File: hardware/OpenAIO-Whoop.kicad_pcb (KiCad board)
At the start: 6 copper layers, 30.5 x 30.5 mm, 0 parts

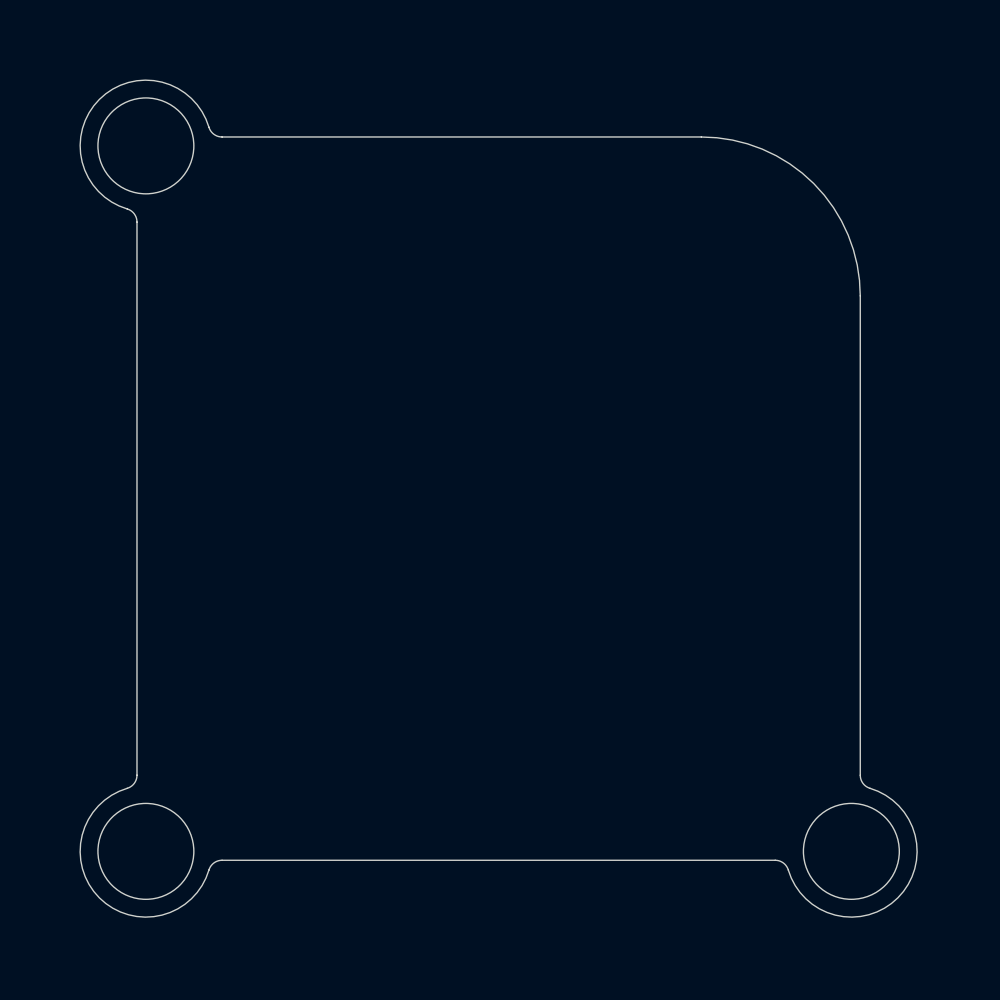
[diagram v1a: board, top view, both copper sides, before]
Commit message: hardware: P2 floorplan run 2 (326/329 placed, 0 spacing, 0 DRC)
Every BOM part placed on its planned side and region with real library
footprints at the 0.2 mm body rule; pad labels, incutec logo and product
name on silk. Compaction with via-in-pad follows.

Co-Authored-By: Claude Opus 5.5 <noreply@anthropic.com>
Claude-Session: https://claude.ai/code/session_01RFaS5jnC9tnPam9GBgmGnG
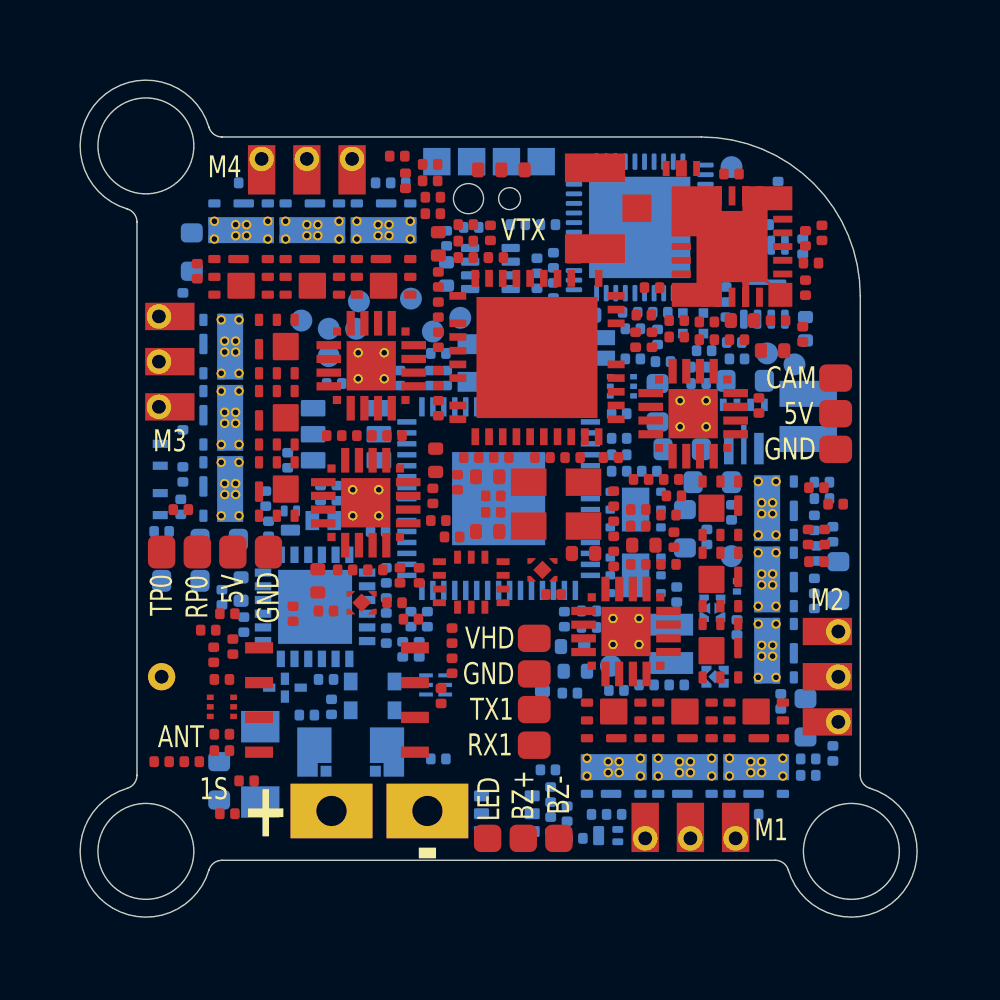
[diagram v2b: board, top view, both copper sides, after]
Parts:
- added AE1: ANT 2.4G wire, lib:AE_WireHole_PTH0.5mm, F.Cu at (100.9, 119.7)
- added C1: 22uF, lib:C_0603_1608Metric_W, B.Cu at (103.0, 123.5)
- added C10: 22uF, lib:C_0603_1608Metric_W, B.Cu at (119.0, 109.7)
- added C100: 100nF, lib:C_0201_0603Metric_W, F.Cu at (112.2, 111.7)
- added C101: 100nF, lib:C_0201_0603Metric_W, F.Cu at (117.3, 111.7)
- added C102: 100pF, lib:C_0201_0603Metric_W, F.Cu at (121.9, 107.4)
- added C103: 100pF, lib:C_0201_0603Metric_W, F.Cu at (112.9, 103.5)
- added C104: 33pF, lib:C_0201_0603Metric_W, F.Cu at (111.0, 105.2)
- added C105: 4.7uF, lib:C_0402_1005Metric_W, F.Cu at (111.0, 103.9)
- added C106: 1uF, lib:C_0402_1005Metric_W, F.Cu at (116.3, 115.2)
- added C107: 4.7uF, lib:C_0402_1005Metric_W, F.Cu at (112.8, 114.4)
- added C108: 10uF, lib:C_0402_1005Metric_W, F.Cu at (112.8, 112.4)
- added C109: 10nF, lib:C_0201_0603Metric_W, F.Cu at (118.8, 107.4)
- added C11: 22uF, lib:C_0603_1608Metric_W, B.Cu at (120.0, 114.3)
- added C110: 10pF, lib:C_0201_0603Metric_W, F.Cu at (120.8, 106.8)
- added C111: 100pF, lib:C_0201_0603Metric_W, F.Cu at (124.4, 103.7)
- added C112: 1nF, lib:C_0201_0603Metric_W, F.Cu at (124.6, 104.6)
- added C113: 100pF, lib:C_0201_0603Metric_W, F.Cu at (118.8, 105.5)
- added C114: 1nF, lib:C_0201_0603Metric_W, F.Cu at (119.7, 107.3)
- added C115: 100pF, lib:C_0201_0603Metric_W, F.Cu at (119.7, 106.7)
- added C116: 1nF, lib:C_0201_0603Metric_W, F.Cu at (120.8, 107.4)
- added C117: 100pF, lib:C_0201_0603Metric_W, F.Cu at (124.4, 105.5)
- added C118: 10uF, lib:C_0402_1005Metric_W, F.Cu at (122.1, 106.7)
- added C119: 10pF, lib:C_0201_0603Metric_W, F.Cu at (121.7, 101.3)
- added C12: 10uF, lib:C_0402_1005Metric_W, B.Cu at (111.3, 105.0)
- added C120: 1uF, lib:C_0201_0603Metric_W, B.Cu at (119.7, 116.7)
- added C121: 1uF, lib:C_0201_0603Metric_W, B.Cu at (116.5, 117.3)
- added C122: 1uF, lib:C_0201_0603Metric_W, F.Cu at (109.4, 117.0)
- added C123: 1uF, lib:C_0201_0603Metric_W, F.Cu at (106.9, 117.3)
- added C124: 100nF, lib:C_0201_0603Metric_W, F.Cu at (103.1, 121.8)
- added C125: 100nF, lib:C_0201_0603Metric_W, F.Cu at (102.8, 118.9)
- added C126: 100nF, lib:C_0201_0603Metric_W, B.Cu at (106.2, 121.1)
- added C127: 100nF, lib:C_0201_0603Metric_W, B.Cu at (115.8, 120.3)
- added C13: 1uF, lib:C_0201_0603Metric_W, B.Cu at (120.8, 114.6)
- added C14: 1uF, lib:C_0201_0603Metric_W, B.Cu at (117.6, 112.2)
- added C15: 10uF, lib:C_0402_1005Metric_W, B.Cu at (124.4, 107.0)
- added C16: 10nF, lib:C_0201_0603Metric_W, B.Cu at (105.5, 111.8)
- added C17: 1uF, lib:C_0201_0603Metric_W, B.Cu at (109.6, 108.8)
- added C18: 2.2uF, lib:C_0402_1005Metric_W, F.Cu at (118.5, 114.9)
- added C19: 100nF, lib:C_0201_0603Metric_W, F.Cu at (118.3, 115.6)
- added C2: 22uF, lib:C_0603_1608Metric_W, B.Cu at (101.6, 116.2)
- added C20: 100nF, lib:C_0201_0603Metric_W, B.Cu at (116.9, 124.7)
- added C21: 100nF, lib:C_0201_0603Metric_W, B.Cu at (118.0, 124.7)
- added C22: 100nF, lib:C_0201_0603Metric_W, B.Cu at (122.4, 124.7)
- added C23: 22uF, lib:C_0603_1608Metric_W, B.Cu at (124.4, 121.2)
- added C24: 2.2uF, lib:C_0402_1005Metric_W, F.Cu at (123.2, 107.8)
- added C25: 100nF, lib:C_0201_0603Metric_W, F.Cu at (122.7, 109.8)
- added C26: 100nF, lib:C_0201_0603Metric_W, B.Cu at (124.7, 117.5)
- added C27: 100nF, lib:C_0201_0603Metric_W, B.Cu at (124.7, 116.4)
- added C28: 100nF, lib:C_0201_0603Metric_W, B.Cu at (124.7, 114.1)
- added C29: 22uF, lib:C_0603_1608Metric_W, B.Cu at (125.6, 116.2)
- added C3: 100nF, lib:C_0201_0603Metric_W, B.Cu at (115.0, 123.1)
- added C30: 2.2uF, lib:C_0402_1005Metric_W, F.Cu at (110.9, 111.8)
- added C31: 100nF, lib:C_0201_0603Metric_W, F.Cu at (110.8, 113.1)
- added C32: 100nF, lib:C_0201_0603Metric_W, B.Cu at (101.7, 106.0)
- added C33: 100nF, lib:C_0201_0603Metric_W, B.Cu at (101.7, 110.4)
- added C34: 100nF, lib:C_0201_0603Metric_W, B.Cu at (101.7, 112.3)
- added C35: 22uF, lib:C_0603_1608Metric_W, B.Cu at (103.0, 114.7)
- added C36: 2.2uF, lib:C_0402_1005Metric_W, F.Cu at (106.6, 116.2)
- added C37: 100nF, lib:C_0201_0603Metric_W, F.Cu at (111.0, 109.9)
- added C38: 100nF, lib:C_0201_0603Metric_W, B.Cu at (109.5, 101.7)
- added C39: 100nF, lib:C_0201_0603Metric_W, B.Cu at (108.4, 101.7)
- added C4: 100nF, lib:C_0201_0603Metric_W, B.Cu at (115.7, 124.7)
- added C40: 100nF, lib:C_0201_0603Metric_W, B.Cu at (104.0, 101.7)
- added C41: 22uF, lib:C_0603_1608Metric_W, B.Cu at (102.0, 104.2)
- added C42: 15pF, lib:C_0201_0603Metric_W, B.Cu at (111.3, 108.8)
- added C43: 15pF, lib:C_0201_0603Metric_W, B.Cu at (114.7, 108.8)
- added C44: 100nF, lib:C_0201_0603Metric_W, B.Cu at (109.1, 116.0)
- added C45: 100nF, lib:C_0201_0603Metric_W, B.Cu at (107.2, 109.0)
- added C46: 100nF, lib:C_0201_0603Metric_W, B.Cu at (111.0, 107.9)
- added C47: 100nF, lib:C_0201_0603Metric_W, B.Cu at (116.0, 109.1)
- added C48: 100nF, lib:C_0201_0603Metric_W, B.Cu at (117.6, 111.6)
- added C49: 100nF, lib:C_0201_0603Metric_W, B.Cu at (115.6, 117.6)
- added C5: 1uF, lib:C_0201_0603Metric_W, B.Cu at (116.0, 125.6)
- added C50: 100nF, lib:C_0201_0603Metric_W, B.Cu at (109.1, 117.1)
- added C51: 100nF, lib:C_0201_0603Metric_W, B.Cu at (114.7, 107.7)
- added C52: 100nF, lib:C_0201_0603Metric_W, B.Cu at (118.7, 112.2)
- added C53: 100nF, lib:C_0201_0603Metric_W, B.Cu at (116.5, 117.9)
- added C54: 100nF, lib:C_0201_0603Metric_W, B.Cu at (110.6, 117.6)
- added C55: 100nF, lib:C_0201_0603Metric_W, B.Cu at (110.0, 117.6)
- added C56: 4.7uF, lib:C_0402_1005Metric_W, B.Cu at (115.9, 118.6)
- added C57: 4.7uF, lib:C_0402_1005Metric_W, B.Cu at (116.0, 119.5)
- added C58: 4.7uF, lib:C_0402_1005Metric_W, B.Cu at (114.8, 119.8)
- added C59: 100nF, lib:C_0201_0603Metric_W, B.Cu at (121.9, 117.9)
- added C6: 100nF, lib:C_0201_0603Metric_W, B.Cu at (111.0, 122.7)
- added C60: 100nF, lib:C_0201_0603Metric_W, B.Cu at (119.2, 108.2)
- added C61: 1uF, lib:C_0201_0603Metric_W, F.Cu at (115.2, 116.7)
- added C62: 1uF, lib:C_0201_0603Metric_W, F.Cu at (117.4, 115.4)
- added C63: 100nF, lib:C_0201_0603Metric_W, F.Cu at (110.3, 116.0)
- added C64: 100nF, lib:C_0201_0603Metric_W, F.Cu at (111.5, 114.6)
- added C65: 100nF, lib:C_0201_0603Metric_W, F.Cu at (110.0, 117.6)
- added C66: 100pF, lib:C_0201_0603Metric_W, B.Cu at (123.5, 120.6)
- added C67: 470pF, lib:C_0201_0603Metric_W, B.Cu at (125.4, 122.5)
- added C68: 1uF, lib:C_0201_0603Metric_W, B.Cu at (124.5, 123.3)
- added C69: 100nF, lib:C_0201_0603Metric_W, F.Cu at (124.8, 115.5)
- added C7: 22uF, lib:C_0603_1608Metric_W, B.Cu at (122.2, 108.9)
- added C70: 100nF, lib:C_0201_0603Metric_W, F.Cu at (125.1, 114.6)
- added C71: 15pF, lib:C_0201_0603Metric_W, B.Cu at (118.1, 107.0)
- added C72: 15pF, lib:C_0201_0603Metric_W, B.Cu at (119.1, 106.4)
- added C73: 1uF, lib:C_0201_0603Metric_W, B.Cu at (113.9, 103.2)
- added C74: 100nF, lib:C_0201_0603Metric_W, B.Cu at (115.2, 105.6)
- added C75: 100nF, lib:C_0201_0603Metric_W, B.Cu at (118.0, 106.4)
- added C76: 100nF, lib:C_0201_0603Metric_W, B.Cu at (115.2, 104.5)
- added C77: 10nF, lib:C_0201_0603Metric_W, B.Cu at (114.6, 104.7)
- added C78: 100nF, lib:C_0201_0603Metric_W, B.Cu at (115.0, 103.2)
- added C79: 100nF, lib:C_0201_0603Metric_W, B.Cu at (121.5, 105.2)
- added C8: 22uF, lib:C_0603_1608Metric_W, B.Cu at (121.0, 112.6)
- added C80: 1uF, lib:C_0201_0603Metric_W, B.Cu at (121.7, 103.1)
- added C81: 100nF, lib:C_0201_0603Metric_W, B.Cu at (124.3, 104.0)
- added C82: 10uF, lib:C_0402_1005Metric_W, B.Cu at (116.3, 106.5)
- added C83: 100nF, lib:C_0201_0603Metric_W, B.Cu at (120.7, 107.8)
- added C84: 1nF, lib:C_0201_0603Metric_W, B.Cu at (103.1, 116.8)
- added C85: 100nF, lib:C_0201_0603Metric_W, B.Cu at (107.1, 120.8)
- added C86: 10nF, lib:C_0201_0603Metric_W, B.Cu at (103.9, 117.8)
- added C87: 470nF, lib:C_0201_0603Metric_W, B.Cu at (104.8, 114.3)
- added C88: 10nF, lib:C_0201_0603Metric_W, B.Cu at (109.1, 118.2)
- added C89: 100nF, lib:C_0201_0603Metric_W, B.Cu at (109.7, 118.7)
- added C9: 22uF, lib:C_0603_1608Metric_W, B.Cu at (119.9, 111.4)
- added C90: 10nF, lib:C_0201_0603Metric_W, B.Cu at (110.3, 118.7)
- added C91: 100nF, lib:C_0201_0603Metric_W, B.Cu at (104.7, 113.2)
- added C92: 1uF, lib:C_0201_0603Metric_W, B.Cu at (106.9, 119.8)
- added C93: 10uF, lib:C_0402_1005Metric_W, B.Cu at (103.8, 116.5)
- added C94: 15pF, lib:C_0201_0603Metric_W, F.Cu at (115.9, 111.7)
- added C95: 15pF, lib:C_0201_0603Metric_W, F.Cu at (113.0, 113.1)
- added C96: 470nF, lib:C_0201_0603Metric_W, F.Cu at (113.3, 111.7)
- added C97: 100nF, lib:C_0201_0603Metric_W, F.Cu at (114.8, 111.7)
- added C98: 100nF, lib:C_0201_0603Metric_W, F.Cu at (113.1, 104.4)
- added C99: 100nF, lib:C_0201_0603Metric_W, F.Cu at (111.0, 108.8)
- added D1: SMF5.0A, lib:SOD-123FL_L2.7-W1.8-LS3.7-RD_Dense, B.Cu at (104.5, 122.9)
- added D2: BAS16LD, lib:Nexperia_SOD882D, B.Cu at (106.8, 114.0)
- added D3: SDM02U30LP3, lib:X3-DFN0603-2_L0.6-W0.3-RD_W, B.Cu at (121.9, 116.4)
- added D4: RGB WS2812, lib:LED-SMD_4P-L1.0-W1.0-TL_XL-1010RGBC-WS2812B_Dense, B.Cu at (120.3, 106.8)
- added D5: green, lib:LED_0402_1005Metric, B.Cu at (100.8, 111.6)
- added D6: blue, lib:LED_0402_1005Metric, B.Cu at (100.8, 113.4)
- added FB1: 120R@100MHz 0.9A, lib:L_0201_0603Metric_W, B.Cu at (121.8, 107.5)
- added FL1: LPF 2.4G, lib:FILTER-SMD_4P-L1.0-W0.5-L_DEA102700LT-XXX_W, B.Cu at (105.4, 120.1)
- added FL2: BPF 5.15-5.95G, lib:Walsin_RFBPF1608060K98Q1C, F.Cu at (119.9, 101.2)
- added J1: U.FL, lib:U.FL_Hirose_U.FL-R-SMT-1_Vertical, F.Cu at (116.7, 102.6)
- added J10: M3, lib:MotorPad_1.0x1.8mm_PTH0.5, F.Cu at (101.2, 106.5)
- added J11: M3, lib:MotorPad_1.0x1.8mm_PTH0.5, F.Cu at (101.2, 108.2)
- added J12: M3, lib:MotorPad_1.0x1.8mm_PTH0.5, F.Cu at (101.2, 109.8)
- added J13: M4, lib:MotorPad_1.0x1.8mm_PTH0.5, F.Cu at (104.5, 101.2)
- added J14: M4, lib:MotorPad_1.0x1.8mm_PTH0.5, F.Cu at (106.2, 101.2)
- added J15: M4, lib:MotorPad_1.0x1.8mm_PTH0.5, F.Cu at (107.8, 101.2)
- added J16: TP0, lib:SolderPad_1.0x1.2mm, F.Cu at (100.9, 115.2)
- added J17: RP0, lib:SolderPad_1.0x1.2mm, F.Cu at (102.2, 115.2)
- added J18: 5V, lib:SolderPad_1.0x1.2mm, F.Cu at (103.5, 115.2)
- added J19: GND, lib:SolderPad_1.0x1.2mm, F.Cu at (104.8, 115.2)
- added J2: +, lib:BattPad_3.0x2.0mm_PTH1.1, F.Cu at (107.1, 124.6)
- added J20: LED, lib:SolderPad_1.0x1.2mm_Dense, F.Cu at (112.8, 125.6)
- added J21: BZ+, lib:SolderPad_1.0x1.2mm_Dense, F.Cu at (114.1, 125.6)
- added J22: BZ-, lib:SolderPad_1.0x1.2mm_Dense, F.Cu at (115.4, 125.6)
- added J23: CAM, lib:SolderPad_1.0x1.2mm, F.Cu at (125.5, 108.8)
- added J24: 5V, lib:SolderPad_1.0x1.2mm, F.Cu at (125.5, 110.1)
- added J25: GND, lib:SolderPad_1.0x1.2mm, F.Cu at (125.5, 111.4)
- added J26: VHD, lib:SolderPad_1.0x1.2mm, F.Cu at (114.5, 118.3)
- added J27: GND, lib:SolderPad_1.0x1.2mm, F.Cu at (114.5, 119.6)
- added J28: TX1, lib:SolderPad_1.0x1.2mm, F.Cu at (114.5, 120.9)
- added J29: RX1, lib:SolderPad_1.0x1.2mm, F.Cu at (114.5, 122.2)
- added J3: -, lib:BattPad_3.0x2.0mm_PTH1.1, F.Cu at (110.6, 124.6)
- added J30: USB pogo, lib:USB_Pogo_4x1.0mm_NPTH0.8_1.1, B.Cu at (112.8, 100.9)
- added J4: M1, lib:MotorPad_1.0x1.8mm_PTH0.5, F.Cu at (118.5, 125.2)
- added J5: M1, lib:MotorPad_1.0x1.8mm_PTH0.5, F.Cu at (120.2, 125.2)
- added J6: M1, lib:MotorPad_1.0x1.8mm_PTH0.5, F.Cu at (121.8, 125.2)
- added J7: M2, lib:MotorPad_1.0x1.8mm_PTH0.5, F.Cu at (125.2, 118.0)
- added J8: M2, lib:MotorPad_1.0x1.8mm_PTH0.5, F.Cu at (125.2, 119.7)
- added J9: M2, lib:MotorPad_1.0x1.8mm_PTH0.5, F.Cu at (125.2, 121.3)
- added L1: 0.68uH 6.5A, lib:IND-SMD_L2.5-W2.0_FTC252012, B.Cu at (124.5, 110.2)
- added L2: 3.3uH, lib:IND-SMD_L2.0-W1.6_AOTA-B201610S3R3-101-T_Dense, B.Cu at (119.5, 118.5)
- added L3: 4.7nH, lib:L_0201_0603Metric_W, F.Cu at (118.2, 107.4)
- added LOGO1: incutec, lib:incutec_logo_6.1x1.4mm, B.Cu at (120.0, 121.4)
- added Q1: AP1606, lib:DFN-3L_L1.0-W0.6-P0.65-BR_W, B.Cu at (105.6, 114.0)
- added Q10: CSD25310Q2, lib:TI_SON-6_2x2mm_CSD25310Q2, F.Cu at (121.3, 113.5)
- added Q11: CSD13202Q2, lib:TI_SON-6_2x2mm_DQK_CSD13202Q2, B.Cu at (123.3, 118.8)
- added Q12: CSD13202Q2, lib:TI_SON-6_2x2mm_DQK_CSD13202Q2, B.Cu at (123.3, 116.2)
- added Q13: CSD13202Q2, lib:TI_SON-6_2x2mm_DQK_CSD13202Q2, B.Cu at (123.3, 113.5)
- added Q14: CSD25310Q2, lib:TI_SON-6_2x2mm_CSD25310Q2, F.Cu at (105.1, 107.7)
- added Q15: CSD25310Q2, lib:TI_SON-6_2x2mm_CSD25310Q2, F.Cu at (105.1, 110.2)
- added Q16: CSD25310Q2, lib:TI_SON-6_2x2mm_CSD25310Q2, F.Cu at (105.1, 112.8)
- added Q17: CSD13202Q2, lib:TI_SON-6_2x2mm_DQK_CSD13202Q2, B.Cu at (103.1, 107.7)
- added Q18: CSD13202Q2, lib:TI_SON-6_2x2mm_DQK_CSD13202Q2, B.Cu at (103.1, 110.2)
- added Q19: CSD13202Q2, lib:TI_SON-6_2x2mm_DQK_CSD13202Q2, B.Cu at (103.1, 112.8)
- added Q2: CSD25310Q2, lib:TI_SON-6_2x2mm_CSD25310Q2, F.Cu at (117.4, 121.3)
- added Q20: CSD25310Q2, lib:TI_SON-6_2x2mm_CSD25310Q2, F.Cu at (109.0, 105.1)
- added Q21: CSD25310Q2, lib:TI_SON-6_2x2mm_CSD25310Q2, F.Cu at (106.4, 105.1)
- added Q22: CSD25310Q2, lib:TI_SON-6_2x2mm_CSD25310Q2, F.Cu at (103.8, 105.1)
- added Q23: CSD13202Q2, lib:TI_SON-6_2x2mm_DQK_CSD13202Q2, B.Cu at (109.0, 103.1)
- added Q24: CSD13202Q2, lib:TI_SON-6_2x2mm_DQK_CSD13202Q2, B.Cu at (106.4, 103.1)
- added Q25: CSD13202Q2, lib:TI_SON-6_2x2mm_DQK_CSD13202Q2, B.Cu at (103.8, 103.1)
- added Q26: AP1606, lib:DFN-3L_L1.0-W0.6-P0.65-BR_W, B.Cu at (117.2, 125.5)
- added Q27: BC847QAS, lib:Nexperia_DFN1010B-6_SOT1216, F.Cu at (103.1, 120.8)
- added Q28: BC847QAS, lib:Nexperia_DFN1010B-6_SOT1216, B.Cu at (117.7, 109.1)
- added Q3: CSD25310Q2, lib:TI_SON-6_2x2mm_CSD25310Q2, F.Cu at (120.0, 121.3)
- added Q4: CSD25310Q2, lib:TI_SON-6_2x2mm_CSD25310Q2, F.Cu at (122.6, 121.3)
- added Q5: CSD13202Q2, lib:TI_SON-6_2x2mm_DQK_CSD13202Q2, B.Cu at (117.4, 123.3)
- added Q6: CSD13202Q2, lib:TI_SON-6_2x2mm_DQK_CSD13202Q2, B.Cu at (120.0, 123.3)
- added Q7: CSD13202Q2, lib:TI_SON-6_2x2mm_DQK_CSD13202Q2, B.Cu at (122.6, 123.3)
- added Q8: CSD25310Q2, lib:TI_SON-6_2x2mm_CSD25310Q2, F.Cu at (121.3, 118.8)
- added Q9: CSD25310Q2, lib:TI_SON-6_2x2mm_CSD25310Q2, F.Cu at (121.3, 116.2)
- added R1: 0.5mR 2W, lib:R_1206_Kelvin_4Pad_NetTie_HCS1206_Dense, B.Cu at (107.8, 122.5)
- added R10: 49.9k, lib:R_0201_0603Metric_W, B.Cu at (106.7, 113.0)
- added R11: 4.7k, lib:R_0201_0603Metric_W, B.Cu at (108.8, 114.4)
- added R12: 2.4k, lib:R_0201_0603Metric_W, F.Cu at (119.4, 115.6)
- added R13: 10k, lib:R_0201_0603Metric_W, F.Cu at (117.4, 114.3)
- added R14: 10k, lib:R_0201_0603Metric_W, F.Cu at (119.6, 114.7)
- added R15: 10k, lib:R_0201_0603Metric_W, F.Cu at (118.3, 114.2)
- added R16: 1k, lib:R_0201_0603Metric_W, F.Cu at (118.3, 113.6)
- added R17: 1k, lib:R_0201_0603Metric_W, F.Cu at (119.4, 113.8)
- added R18: 1k, lib:R_0201_0603Metric_W, F.Cu at (117.4, 113.2)
- added R19: 2.4k, lib:R_0201_0603Metric_W, F.Cu at (119.5, 112.5)
- added R2: 1k, lib:R_0201_0603Metric_W, B.Cu at (115.1, 124.0)
- added R20: 10k, lib:R_0201_0603Metric_W, F.Cu at (118.4, 112.5)
- added R21: 10k, lib:R_0201_0603Metric_W, F.Cu at (119.6, 113.1)
- added R22: 10k, lib:R_0201_0603Metric_W, F.Cu at (124.3, 107.2)
- added R23: 1k, lib:R_0201_0603Metric_W, F.Cu at (124.8, 112.8)
- added R24: 1k, lib:R_0201_0603Metric_W, F.Cu at (124.5, 114.6)
- added R25: 1k, lib:R_0201_0603Metric_W, F.Cu at (125.5, 113.4)
- added R26: 2.4k, lib:R_0201_0603Metric_W, F.Cu at (107.6, 115.8)
- added R27: 10k, lib:R_0201_0603Metric_W, F.Cu at (108.3, 110.9)
- added R28: 10k, lib:R_0201_0603Metric_W, F.Cu at (108.7, 115.8)
- added R29: 10k, lib:R_0201_0603Metric_W, F.Cu at (107.2, 110.9)
- added R3: 1k, lib:R_0201_0603Metric_W, B.Cu at (115.1, 125.1)
- added R30: 1k, lib:R_0201_0603Metric_W, F.Cu at (109.4, 110.9)
- added R31: 1k, lib:R_0201_0603Metric_W, F.Cu at (111.0, 114.0)
- added R32: 1k, lib:R_0201_0603Metric_W, F.Cu at (109.6, 116.0)
- added R33: 2.4k, lib:R_0201_0603Metric_W, F.Cu at (102.2, 104.9)
- added R34: 10k, lib:R_0201_0603Metric_W, F.Cu at (110.8, 102.8)
- added R35: 10k, lib:R_0201_0603Metric_W, F.Cu at (110.8, 102.2)
- added R36: 10k, lib:R_0201_0603Metric_W, F.Cu at (109.8, 101.6)
- added R37: 1k, lib:R_0201_0603Metric_W, F.Cu at (110.7, 101.6)
- added R38: 1k, lib:R_0201_0603Metric_W, F.Cu at (110.7, 101.0)
- added R39: 1k, lib:R_0201_0603Metric_W, F.Cu at (109.5, 100.7)
- added R4: 909k, lib:R_0201_0603Metric_W, B.Cu at (120.5, 109.0)
- added R40: 1k, lib:R_0201_0603Metric_W, B.Cu at (110.7, 108.8)
- added R41: 30R, lib:R_0201_0603Metric_W, B.Cu at (119.7, 120.0)
- added R42: 27R, lib:R_0201_0603Metric_W, B.Cu at (118.6, 120.0)
- added R43: 27R, lib:R_0201_0603Metric_W, F.Cu at (111.5, 119.3)
- added R44: 1k, lib:R_0201_0603Metric_W, F.Cu at (111.1, 120.4)
- added R45: 10k, lib:R_0201_0603Metric_W, B.Cu at (117.6, 111.0)
- added R46: 10k, lib:R_0201_0603Metric_W, B.Cu at (121.7, 113.7)
- added R47: 1k, lib:R_0201_0603Metric_W, B.Cu at (115.3, 108.2)
- added R48: 100k, lib:R_0201_0603Metric_W, B.Cu at (117.5, 120.2)
- added R49: 10k, lib:R_0201_0603Metric_W, F.Cu at (111.5, 118.2)
- added R5: 120k, lib:R_0201_0603Metric_W, B.Cu at (120.5, 108.4)
- added R50: 10k, lib:R_0201_0603Metric_W, F.Cu at (103.5, 118.6)
- added R51: 75R, lib:R_0201_0603Metric_W, B.Cu at (124.8, 115.2)
- added R52: 820R, lib:R_0201_0603Metric_W, B.Cu at (125.4, 114.5)
- added R53: 2.4k, lib:R_0201_0603Metric_W, B.Cu at (125.0, 113.2)
- added R54: 287R, lib:R_0201_0603Metric_W, B.Cu at (125.0, 112.6)
- added R55: 680R, lib:R_0201_0603Metric_W, B.Cu at (124.5, 122.7)
- added R56: 10k, lib:R_0201_0603Metric_W, B.Cu at (114.6, 105.8)
- added R57: 51R, lib:R_0402_1005Metric, B.Cu at (113.5, 106.4)
- added R58: 1.2k, lib:R_0201_0603Metric_W, F.Cu at (112.0, 104.4)
- added R59: 270R, lib:R_0201_0603Metric_W, F.Cu at (112.0, 103.8)
- added R6: 100k, lib:R_0201_0603Metric_W, B.Cu at (121.9, 108.1)
- added R60: 1.2k, lib:R_0201_0603Metric_W, F.Cu at (111.0, 106.3)
- added R61: 510k, lib:R_0201_0603Metric_W, F.Cu at (112.0, 103.2)
- added R62: 560k, lib:R_0201_0603Metric_W, F.Cu at (111.0, 107.4)
- added R63: 100k, lib:R_0201_0603Metric_W, F.Cu at (113.0, 113.7)
- added R64: 47k, lib:R_0201_0603Metric_W, F.Cu at (111.7, 112.6)
- added R65: 10R, lib:R_0201_0603Metric_W, F.Cu at (118.5, 106.5)
- added R66: 1k, lib:R_0201_0603Metric_W, F.Cu at (125.0, 103.5)
- added R67: 0R, lib:R_0402_Selector_3Pad, F.Cu at (113.3, 101.2)
- added R68: 100k, lib:R_0201_0603Metric_W, F.Cu at (103.3, 124.7)
- added R69: 10k, lib:R_0201_0603Metric_W, F.Cu at (105.7, 117.4)
- added R7: 27.4k, lib:R_0201_0603Metric_W, B.Cu at (112.2, 103.3)
- added R70: 10k, lib:R_0201_0603Metric_W, F.Cu at (101.6, 113.6)
- added R71: 18k, lib:R_0201_0603Metric_W, F.Cu at (103.1, 119.8)
- added R72: 18k, lib:R_0201_0603Metric_W, F.Cu at (103.1, 122.4)
- added R73: 10k, lib:R_0201_0603Metric_W, F.Cu at (102.0, 122.8)
- added R74: 6.2k, lib:R_0201_0603Metric_W, F.Cu at (100.9, 122.8)
- added R75: 150R, lib:R_0201_0603Metric_W, F.Cu at (102.6, 118.0)
- added R76: 1k, lib:R_0201_0603Metric_W, F.Cu at (104.0, 123.5)
- added R77: 3.3k, lib:R_0201_0603Metric_W, F.Cu at (103.3, 117.4)
- added R78: 10k, lib:R_0201_0603Metric_W, B.Cu at (117.6, 110.1)
- added R79: 10k, lib:R_0201_0603Metric_W, B.Cu at (118.1, 108.1)
- added R8: 10k, lib:R_0201_0603Metric_W, B.Cu at (111.3, 103.7)
- added R80: 1k, lib:R_0201_0603Metric_W, B.Cu at (121.5, 106.3)
- added R81: 1k, lib:R_0201_0603Metric_W, B.Cu at (121.5, 104.1)
- added R82: 1k, lib:R_0201_0603Metric_W, B.Cu at (122.8, 103.2)
- added R83: 1k, lib:R_0201_0603Metric_W, B.Cu at (123.4, 101.9)
- added R84: 10k, lib:R_0201_0603Metric_W, B.Cu at (119.0, 107.3)
- added R85: 150R, lib:R_0201_0603Metric_W, B.Cu at (101.6, 113.5)
- added R86: 150R, lib:R_0201_0603Metric_W, B.Cu at (100.9, 114.4)
- added R9: 80.6k, lib:R_0201_0603Metric_W, B.Cu at (107.3, 113.0)
- added TH1: 10k NTC B3380, lib:R_0201_0603Metric_W, F.Cu at (123.4, 106.7)
- added TP1: C2D, lib:TestPoint_Pad_D0.8mm, B.Cu at (117.3, 119.3)
- added TP10: GND, lib:TestPoint_Pad_D0.8mm, B.Cu at (107.0, 108.0)
- added TP11: RXB, lib:TestPoint_Pad_D0.8mm, B.Cu at (121.7, 101.1)
- added TP12: CLK, lib:TestPoint_Pad_D0.8mm, B.Cu at (108.0, 107.0)
- added TP13: DIO, lib:TestPoint_Pad_D0.8mm, B.Cu at (106.0, 106.7)
- added TP2: C2CK, lib:TestPoint_Pad_D0.8mm, B.Cu at (121.7, 115.3)
- added TP3: C2D, lib:TestPoint_Pad_D0.8mm, B.Cu at (123.0, 107.9)
- added TP4: C2CK, lib:TestPoint_Pad_D0.8mm, B.Cu at (124.0, 108.3)
- added TP5: C2D, lib:TestPoint_Pad_D0.8mm, B.Cu at (110.8, 107.1)
- added TP6: C2CK, lib:TestPoint_Pad_D0.8mm, B.Cu at (111.8, 106.6)
- added TP7: C2D, lib:TestPoint_Pad_D0.8mm, B.Cu at (110.0, 105.9)
- added TP8: C2CK, lib:TestPoint_Pad_D0.8mm, B.Cu at (108.1, 106.0)
- added TP9: FCB, lib:TestPoint_Pad_D0.8mm, B.Cu at (107.0, 107.0)
- added U1: INA186A3, lib:SOT-363_SC-70-6_Dense, B.Cu at (113.5, 124.7)
- added U10: RP2354A, lib:QFN-60_L7.0-W7.0-P0.40-TL-EP3.4_Dense, B.Cu at (113.2, 113.2)
- added U11: BMI270, lib:LGA-14_L3.0-W2.5-P0.50-BR_W, F.Cu at (112.2, 116.2)
- added U12: TPS7A2018, lib:X2SON-4_L1.0-W1.0-P0.65-TL-EP_Dense, F.Cu at (114.8, 115.8)
- added U13: W25Q128JVPIM, lib:WSON-8_6x5mm_P1.27mm_NoEP, F.Cu at (107.3, 120.5)
- added U14: SN74LVC1G3157, lib:X2SON-6_L1.0-W0.8-BL_Dense, B.Cu at (121.0, 117.2)
- added U15: TLV7031, lib:X2SON-4_L0.8-W0.8-P0.48-TL-A_Dense, B.Cu at (121.1, 119.7)
- added U16: ESP32-D0WD-V3, lib:QFN-48_5x5mm_P0.35mm_EP_ESP32-D0WD, B.Cu at (118.3, 103.3)
- added U17: GD25Q32EEIGR, lib:USON-8_3x2mm_P0.5mm_EP_GD25Q32E, B.Cu at (122.9, 105.3)
- added U18: SX1280, lib:QFN-24_L4.0-W4.0-P0.50-TL-EP2.6_Dense, B.Cu at (106.5, 117.2)
- added U19: RTC6705, lib:QFN-40_6x6mm_P0.5mm_EP_RTC6705_Dense, F.Cu at (114.6, 108.0)
- added U2: TPS61022, lib:TI_VQFN-HR-7_2x2mm_RWU, B.Cu at (122.2, 110.8)
- added U20: SE5004L, lib:QFN-20_4x4mm_P0.5mm_EP_SE5004L, F.Cu at (121.7, 104.0)
- added U21: LP5912-3.3, lib:WSON-6-1EP_2x2mm_P0.65mm_EP1x1.6mm_Dense, B.Cu at (118.2, 116.0)
- added U22: LP5907-2.85, lib:X2SON-4_L1.0-W1.0-P0.65-TL-EP_Dense, F.Cu at (108.2, 117.0)
- added U23: 74LVC1T45, lib:Nexperia_XSON6_SOT1202_1x1mm, B.Cu at (110.9, 120.0)
- added U3: TPS2116, lib:TI_SOT-583_DRL, B.Cu at (112.9, 104.8)
- added U4: LP5912-3.3, lib:WSON-6-1EP_2x2mm_P0.65mm_EP1x1.6mm_Dense, B.Cu at (118.2, 113.6)
- added U5: TPS22810, lib:SOT-23-6_L2.9-W1.6-P0.95-LS2.8-BR_Dense, B.Cu at (107.6, 110.8)
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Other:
- board text added: "+"
- board text added: "-"
- board text added: "1S"
- board text added: "5V"
- board text added: "AIO"
- board text added: "ANT"
- board text added: "BZ+"
- board text added: "BZ-"
- board text added: "CAM"
- board text added: "CLK"
- board text added: "DIO"
- board text added: "FCB"
- board text added: "GND"
- board text added: "LED"
- board text added: "M1"
- board text added: "M2"
- board text added: "M3"
- board text added: "M4"
- board text added: "OPEN"
- board text added: "REV1"
- board text added: "RP0"
- board text added: "RX1"
- board text added: "RXB"
- board text added: "TP0"
- board text added: "TX1"
- board text added: "USB"
- board text added: "VHD"
- board text added: "VTX"
- board text added: "WHOOP"

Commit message: hardware: P2 floorplan compaction pass (via-in-pad counted, empty patches closed)
Co-Authored-By: Claude Opus 5.5 <noreply@anthropic.com>
Claude-Session: https://claude.ai/code/session_01RFaS5jnC9tnPam9GBgmGnG
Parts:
- moved C103 9.81 mm to (121.9, 107.4), turned to 0 degrees
- moved R45 9.13 mm to (116.9, 120.1)
- moved C102 8.44 mm to (114.0, 104.5)
- moved C67 8.00 mm to (125.4, 114.5)
- moved C68 7.89 mm to (120.1, 116.8), turned to 90 degrees
- moved R35 7.70 mm to (111.0, 109.9), turned to 90 degrees
- moved R46 7.48 mm to (118.0, 120.2), turned to 0 degrees
- moved C88 6.66 mm to (104.7, 113.2)
- moved C45 6.01 mm to (109.1, 114.7), turned to 90 degrees
- moved R25 5.97 mm to (119.6, 112.5)
- moved C127 5.79 mm to (110.3, 118.5)
- moved R11 5.63 mm to (107.2, 109.0)
- moved R55 5.28 mm to (119.9, 120.1)
- moved R85 4.20 mm to (101.7, 109.3)
- moved C126 3.96 mm to (109.6, 119.1)
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
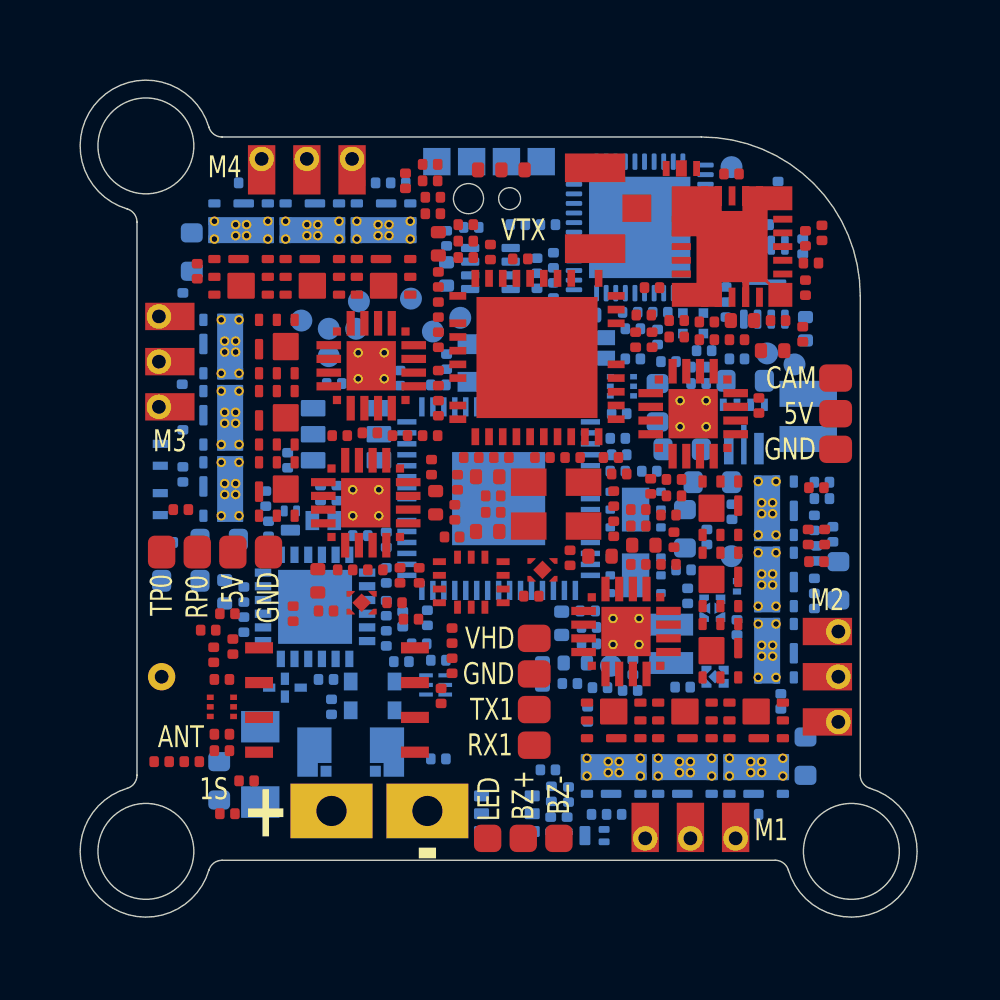
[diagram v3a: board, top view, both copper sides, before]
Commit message: schematic: integrated (ERC 0 errors / 2 justified warnings; check_netlist 7/7; conventions 0 FAIL; visual 0 hits; 268/268 refs match bom_plan; FC+RX pin maps match PINMAP)
Co-Authored-By: Claude Opus 5.5 <noreply@anthropic.com>
Claude-Session: https://claude.ai/code/session_01RFaS5jnC9tnPam9GBgmGnG
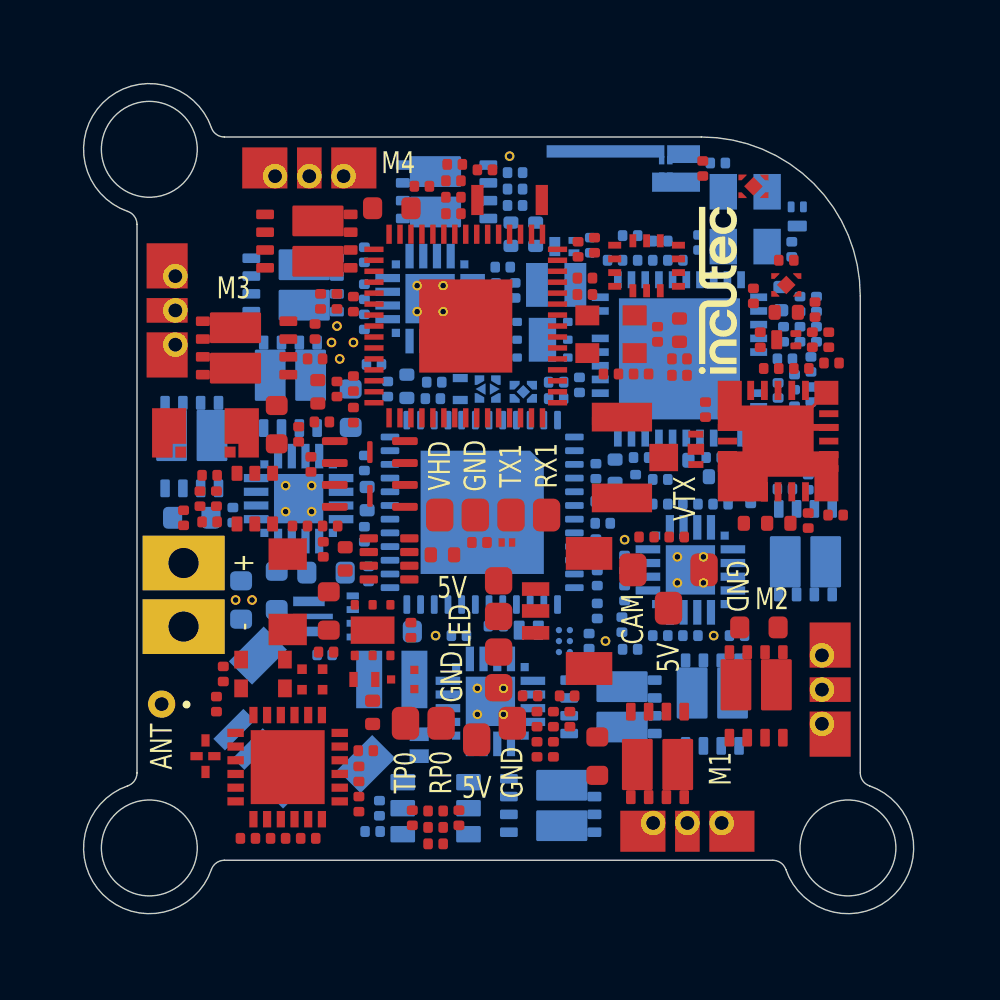
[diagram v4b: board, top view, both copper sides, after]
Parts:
- removed C119: 10pF, lib:C_0201_0603Metric_W
- removed C120, C80: 1uF, lib:C_0201_0603Metric_W
- removed C126, C127, C20, C21, C22, C26, C27, C28, C3, C32, C33, C34, C38, C39, C4, C40, C53, C55, C63, C64, C69, C74, C75, C78, C79, C81, C97, C99: 100nF, lib:C_0201_0603Metric_W
- removed C18, C24, C36: 2.2uF, lib:C_0402_1005Metric_W
- removed C71, C72: 15pF, lib:C_0201_0603Metric_W
- removed C77, C90: 10nF, lib:C_0201_0603Metric_W
- removed C93: 10uF, lib:C_0402_1005Metric_W
- removed J11, J12: M3, lib:MotorPad_1.0x1.8mm_PTH0.5
- removed J14, J15: M4, lib:MotorPad_1.0x1.8mm_PTH0.5
- removed J30: USB pogo, lib:USB_Pogo_4x1.0mm_NPTH0.8_1.1
- removed J5, J6: M1, lib:MotorPad_1.0x1.8mm_PTH0.5
- removed J8, J9: M2, lib:MotorPad_1.0x1.8mm_PTH0.5
- removed Q1: AP1606, lib:DFN-3L_L1.0-W0.6-P0.65-BR_W
- removed Q10, Q14, Q15, Q16, Q2, Q20, Q21, Q22, Q3, Q4, Q8, Q9: CSD25310Q2, lib:TI_SON-6_2x2mm_CSD25310Q2
- removed Q11, Q12, Q13, Q17, Q18, Q19, Q23, Q24, Q25, Q5, Q6, Q7: CSD13202Q2, lib:TI_SON-6_2x2mm_DQK_CSD13202Q2
- removed R57: 51R, lib:R_0402_1005Metric
- removed R6: 100k, lib:R_0201_0603Metric_W
- removed R69, R78, R79: 10k, lib:R_0201_0603Metric_W
- removed R74: 6.2k, lib:R_0201_0603Metric_W
- removed R75: 150R, lib:R_0201_0603Metric_W
- removed R76, R83: 1k, lib:R_0201_0603Metric_W
- removed R77: 3.3k, lib:R_0201_0603Metric_W
- removed TP10: GND, lib:TestPoint_Pad_D0.8mm
- removed TP11: RXB, lib:TestPoint_Pad_D0.8mm
- removed U17: GD25Q32EEIGR, lib:USON-8_3x2mm_P0.5mm_EP_GD25Q32E
- removed U23: 74LVC1T45, lib:Nexperia_XSON6_SOT1202_1x1mm
- removed X2: 40MHz, lib:CRYSTAL-SMD_4P-L1.6-W1.2-BL_Dense
- added AE2: 2450AT07A0100001T, lib:ANT-SMD_4P-L1.0-W0.5_Johanson_2450AT07A0100_Edge5.0x3.2, B.Cu at (119.3, 101.2)
- added C128: 10uF, lib:C_0402_1005Metric_W, F.Cu at (111.2, 115.2)
- added C129: 100nF, lib:C_0201_0603Metric_W, F.Cu at (110.9, 124.6)
- added C131: 100nF, lib:C_0201_0603Metric_W, B.Cu at (116.5, 118.4)
- added C132: 1.2pF, lib:C_0201_0603Metric_W, B.Cu at (118.0, 103.6)
- added C133: 1.2pF, lib:C_0201_0603Metric_W, B.Cu at (121.2, 101.0)
- added C134: 4.7uF, lib:C_0402_1005Metric_W, B.Cu at (109.8, 109.1)
- added D7: TPD2EUSB30, lib:TI_SOT-9X3-3_DRT, F.Cu at (109.7, 119.8)
- added D8: SDM02M30CLP3, lib:X2-DFN1006-3_L1.0-W0.6_SDM02M30CLP3, B.Cu at (115.6, 104.0)
- added J31: USB, lib:CONN-SMD_4P-P1.00_BM04B-SRSS-TB, B.Cu at (105.5, 121.8)
- added J32: CAM, lib:JST_SUR_SM03B-SURS-TF_1x03-1MP_P0.80mm_Horizontal, F.Cu at (115.7, 117.3)
- added J33: GND, lib:SolderPad_1.0x1.2mm_Dense, F.Cu at (113.2, 120.1)
- added Q29: AGM210MAP, lib:AGM_PDFN-8-2EP_3.3x3.3mm_AGM210MAP, B.Cu at (117.3, 120.8)
- added Q30: AGM210MAP, lib:AGM_PDFN-8-2EP_3.3x3.3mm_AGM210MAP, B.Cu at (115.1, 124.4)
- added Q31: AGM210MAP, lib:AGM_PDFN-8-2EP_3.3x3.3mm_AGM210MAP, F.Cu at (119.0, 122.5)
- added Q32: AGM210MAP, lib:AGM_PDFN-8-2EP_3.3x3.3mm_AGM210MAP, B.Cu at (124.4, 115.1)
- added Q33: AGM210MAP, lib:AGM_PDFN-8-2EP_3.3x3.3mm_AGM210MAP, B.Cu at (121.0, 120.7)
- added Q34: AGM210MAP, lib:AGM_PDFN-8-2EP_3.3x3.3mm_AGM210MAP, F.Cu at (122.6, 120.4)
- added Q35: AGM210MAP, lib:AGM_PDFN-8-2EP_3.3x3.3mm_AGM210MAP, B.Cu at (105.6, 109.1)
- added Q36: AGM210MAP, lib:AGM_PDFN-8-2EP_3.3x3.3mm_AGM210MAP, B.Cu at (102.0, 111.3)
- added Q37: AGM210MAP, lib:AGM_PDFN-8-2EP_3.3x3.3mm_AGM210MAP, F.Cu at (104.0, 107.7)
- added Q38: AGM210MAP, lib:AGM_PDFN-8-2EP_3.3x3.3mm_AGM210MAP, B.Cu at (111.3, 102.0)
- added Q39: AGM210MAP, lib:AGM_PDFN-8-2EP_3.3x3.3mm_AGM210MAP, B.Cu at (105.7, 105.4)
- added Q40: AGM210MAP, lib:AGM_PDFN-8-2EP_3.3x3.3mm_AGM210MAP, F.Cu at (106.2, 103.8)
- added R87: 510k, lib:R_0201_0603Metric_W, F.Cu at (110.9, 125.8)
- added R88: 0R, lib:R_0201_0603Metric_W, F.Cu at (120.7, 101.2)
- added SW1: SKUBAAE010, lib:SW_Alps_SKUBAAE010_2.4x1.4mm, F.Cu at (113.6, 102.3)
- added U24: SGM40661, lib:WLCSP-6_L1.30-W0.94-P0.40_SGM40661, B.Cu at (115.6, 118.4)
- C1, C12, C14, C15, C23, C29, C35, C41, C42, C43, C48, C49, C5, C50, C52, C54, C6, C68, C83, C84, C85, C86, C87, C88, C89, C91, C92, D1, D3, D4, D6, FB1, FL1, LOGO1, R1, R10, R11, R2, R3, R40, R41, R42, R45, R46, R47, R48, R55, R7, R8, R84, R9, U1, U10, U18, U3, U4, X1, X3: moved to F.Cu
- C100, C102, C106, C107, C108, C109, C110, C112, C113, C115, C116, C118, C19, C25, C30, C31, C37, C61, C94, C95, C96, C98, L3, R12, R19, R20, R21, R22, R23, R24, R25, R27, R28, R34, R35, R36, R37, R38, R44, R49, R58, R59, R60, R61, R62, R63, R64, R65, R68, R70, U19, U6, U7, U8, U9, X4: moved to B.Cu
- C123: value 1uF -> 4.7uF; footprint lib:C_0201_0603Metric_W -> lib:C_0402_1005Metric_W
- C13: value 1uF -> 10uF; footprint lib:C_0201_0603Metric_W -> lib:C_0402_1005Metric_W; moved to F.Cu
- J10, J13, J4, J7: footprint lib:MotorPad_1.0x1.8mm_PTH0.5 -> lib:MotorPad_PicoBlade_1x03_P1.25mm_PTH0.5
- Q27: value BC847QAS -> BC857BM; footprint lib:Nexperia_DFN1010B-6_SOT1216 -> lib:DFN-3L_L1.0-W0.6-P0.65-BR_W
- Q28: value BC847QAS -> AP1606; footprint lib:Nexperia_DFN1010B-6_SOT1216 -> lib:DFN-3L_L1.0-W0.6-P0.65-BR_W
- TP1, TP2, TP3, TP4, TP7: footprint lib:TestPoint_Pad_D0.8mm -> lib:TestPoint_Via_D0.35mm_Drill0.2mm
- TP12, TP13, TP5, TP6, TP8, TP9: footprint lib:TestPoint_Pad_D0.8mm -> lib:TestPoint_Via_D0.35mm_Drill0.2mm; moved to F.Cu
- U13: value W25Q128JVPIM -> PY25Q128HA-DFH-IR; footprint lib:WSON-8_6x5mm_P1.27mm_NoEP -> lib:USON-8_3x3mm_P0.8mm_EP_PY25Q128HA
- U16: value ESP32-D0WD-V3 -> ESP32-PICO-V3; footprint lib:QFN-48_5x5mm_P0.35mm_EP_ESP32-D0WD -> lib:LGA-48_7x7mm_P0.5mm_EP_ESP32-PICO
- moved R73 27.5 mm to (125.3, 108.2)
- moved R72 26.8 mm to (125.2, 107.4), turned to 90 degrees
- moved R71 25.5 mm to (124.8, 106.3), turned to 90 degrees
- moved C125 24.7 mm to (124.7, 107.4)
- moved Q27 24.6 mm to (123.7, 107.4)
- moved C124 24.4 mm to (122.8, 107.4), turned to 90 degrees
- moved Q26 23.8 mm to (124.1, 102.9), turned to 90 degrees
- moved R70 23.5 mm to (124.2, 107.2), turned to 90 degrees
- moved R48 20.7 mm to (111.6, 101.0), turned to 0 degrees
- moved R68 20.2 mm to (116.2, 109.0), turned to 90 degrees
- moved C123 20.0 mm to (123.7, 106.4)
- moved U22 19.4 mm to (123.7, 105.4)
- moved R41 19.2 mm to (110.4, 101.8), turned to 0 degrees
- moved D4 19.0 mm to (106.4, 119.8)
- moved C122 19.0 mm to (123.7, 104.5)
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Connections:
- J19 pad 1: (no net) -> /FLOORPLAN/GND
- J25 pad 1: (no net) -> /FLOORPLAN/GND
- TP1 pad 1: (no net) -> /FLOORPLAN/TP1_1
- TP12 pad 1: (no net) -> /FLOORPLAN/TP12_1
- TP13 pad 1: (no net) -> /FLOORPLAN/TP13_1
- TP2 pad 1: (no net) -> /FLOORPLAN/TP2_1
- TP3 pad 1: (no net) -> /FLOORPLAN/TP3_1
- TP4 pad 1: (no net) -> /FLOORPLAN/TP4_1
- TP5 pad 1: (no net) -> /FLOORPLAN/TP5_1
- TP6 pad 1: (no net) -> /FLOORPLAN/TP6_1
- TP7 pad 1: (no net) -> /FLOORPLAN/TP7_1
- TP8 pad 1: (no net) -> /FLOORPLAN/TP8_1
- TP9 pad 1: (no net) -> /FLOORPLAN/TP9_1
- U10 pad 61: (no net) -> /FLOORPLAN/GND
- U6 pad 21: /FLOORPLAN/U6_21 -> /FLOORPLAN/GND
- U7 pad 21: /FLOORPLAN/U7_21 -> /FLOORPLAN/GND
- U9 pad 21: /FLOORPLAN/U9_21 -> /FLOORPLAN/GND
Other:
- board size 30.5 x 30.5 mm -> 30.3 x 30.3 mm
- board text added: "ART [F]"
- board text added: "BATT IN [B]"
- board text added: "BATT IN [F]"
- board text added: "BOOST 5 V [B]"
- board text added: "BOOT [B]"
- board text added: "BOOT [F]"
- board text added: "CAM [F]"
- board text added: "ESC1 [B]"
- board text added: "ESC1 [F]"
- board text added: "ESC2 [B]"
- board text added: "ESC2 [F]"
- board text added: "ESC3 [B]"
- board text added: "ESC3 [F]"
- board text added: "ESC4 [B]"
- board text added: "ESC4 [F]"
- board text added: "FC RP2354A [B]"
- board text added: "FC RP2354A [F]"
- board text added: "FC [F]"
- board text added: "HD PADS [F]"
- board text added: "IMU [B]"
- board text added: "IMU [F]"
- board text added: "LED [B]"
- board text added: "LED [F]"
- board text added: "LED/BZ PADS [F]"
- board text added: "MUX + 3V3 [F]"
- board text added: "NOR [F]"
- board text added: "O4 SWITCH [B]"
- board text added: "O4 SWITCH [F]"
- board text added: "OPENAIO WHOOP"
- board text added: "PIO OSD [B]"
- board text added: "PIO OSD [F]"
- board text added: "RX 2.4 GHz [F]"
- board text added: "RX ESP32-PICO [B]"
- board text added: "RX ESP32-PICO [F]"
- board text added: "RX WIRE [F]"
- board text added: "RX wire exit + frame path"
- board text added: "SHUNT + INA [F]"
- board text added: "U.FL coax (VTX antenna)"
- board text added: "UART PADS [F]"
- board text added: "USB [B]"
- board text added: "USB [F]"
- board text added: "VTX PA / RF [B]"
- board text added: "VTX PA / RF [F]"
- board text added: "VTX PWR [B]"
- board text added: "VTX PWR [F]"
- board text added: "VTX RTC6705 [B]"
- board text added: "VTX RTC6705 [F]"
- board text added: "Wi-Fi ANT [B]"
- board text added: "Wi-Fi ANT [F]"
- board text added: "Wi-Fi antenna field"
- board text removed: "1S"
- board text removed: "AIO"
- board text removed: "BZ+"
- board text removed: "BZ-"
- board text removed: "CLK"
- board text removed: "DIO"
- board text removed: "FCB"
- board text removed: "OPEN"
- board text removed: "RXB"
- board text removed: "WHOOP"
